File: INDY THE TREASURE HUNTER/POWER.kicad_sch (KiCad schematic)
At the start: 0 parts

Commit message: 23:43
Working on H-Bridge
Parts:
- added BT1, BT2: Battery, symbol Device:Battery
- added C1, C3: 0.1u, symbol Device:C
- added C2, C4: 2.2u, symbol Device:C
- added U5: LF33_TO220, Package_TO_SOT_THT:TO-220-3_Vertical, symbol Regulator_Linear:LF33_TO220
- added U6: LF50_TO220, Package_TO_SOT_THT:TO-220-3_Vertical, symbol Regulator_Linear:LF50_TO220
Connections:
- net 3V3IN: now also C2.1, U5.3 (VO)
- net 5V: now also C4.1, U6.3 (VO)
- new net: BT1.2 (-), BT2.1 (+)
- new net +BATT: BT1.1 (+), C1.1, C3.1, U5.1 (VI), U6.1 (VI)
- new net GND: BT2.2 (-), C1.2, C2.2, C3.2, C4.2, U5.2 (GND), U6.2 (GND)
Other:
- note added: "3v3 Vregulator"
- note added: "5V Vregulator"
- note added: "Im certain we have more than enough volts to voltage a regulator"

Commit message: 00:53
Battery = done (?)
Motor control = done (no clue)
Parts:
- BT1, BT2: value Battery -> 3.7V
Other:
- note added: "Battery should operate AROUND 7,3V I imagine. Design doesnt need longevity of battery life, so we can assume full charge for a test run, but lets just keep it around the 7,2V mark to be safe. Still, I think the regulators should have more than enough power"
- note removed: "Im certain we have more than enough volts to voltage a regulator"
- moved on the sheet: C1, C2, C3, C4, U5, U6

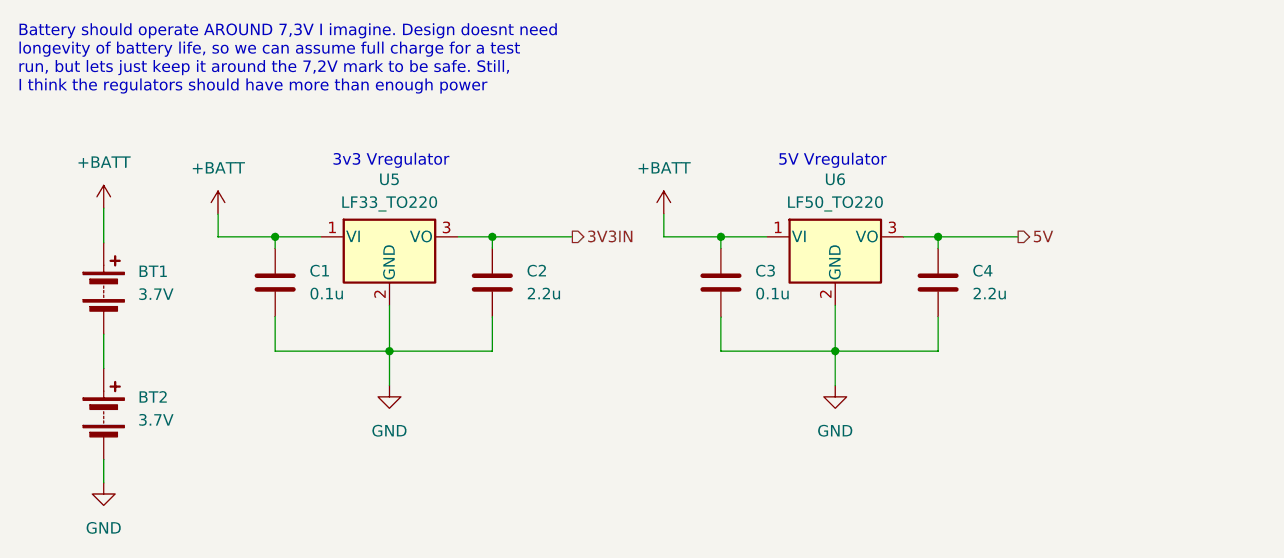
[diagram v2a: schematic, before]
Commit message: No 3V3 regulator
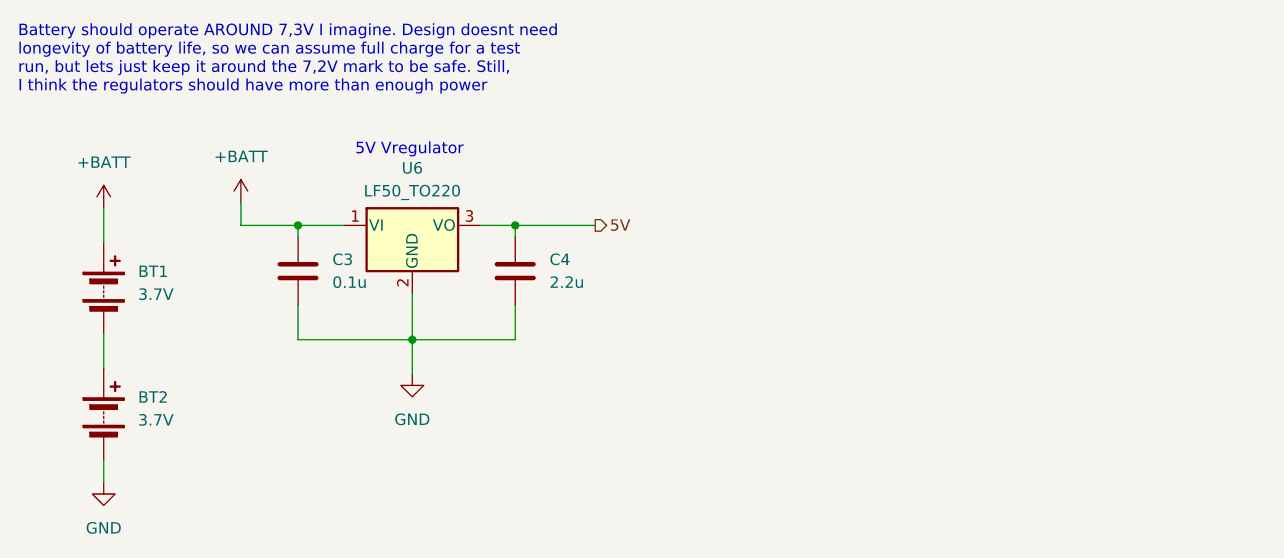
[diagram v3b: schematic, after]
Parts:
- removed C1: 0.1u, symbol Device:C
- removed C2: 2.2u, symbol Device:C
- removed U5: LF33_TO220, Package_TO_SOT_THT:TO-220-3_Vertical, symbol Regulator_Linear:LF33_TO220
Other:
- note removed: "3v3 Vregulator"
- moved on the sheet: C3, C4, U6
